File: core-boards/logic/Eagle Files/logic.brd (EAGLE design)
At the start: 94.2 x 80.9 mm, 78 parts, among them J1 S3B-VH, J2 B2PS-VH(LF)(SN), J3 B2PS-VH(LF)(SN), J4 B2PS-VH(LF)(SN), J5 B2PS-VH(LF)(SN), J6 B2PS-VH(LF)(SN), Q4 STT4P3LLH6, T1 R-78E5.0-1.0, U1 TC4427ACOA713, U2 TXB0106PWRPW16-M, U3 INA198AIDBVR, U4 TLV70233DBVR, U5 MCP2562-I/SN, U6 BMI088, U7 INA198AIDBVR, X1 MINI-USB_SHIELD5P4-32005-400, X10 S6B-EH(LF)(SN), X11 S3B-EH(LF)(SN), X12 B6B-EH-A(LF)(SN), X2 S5B-EH, X3 S5B-EH, X4 B6B-EH-A(LF)(SN), X7 SI-50170, X8 B6B-EH-A(LF)(SN), X9 B6B-EH-A(LF)(SN)

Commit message: logic board revision schemaitcs done
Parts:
- removed C14, C15: 100nF, rcl:C0603
- removed C3: 0.1uF, rcl:C0603
- removed R11: 120, rcl:R0603
- removed R15: 1k, rcl:R0603
- removed R16, R17: (no value), rcl:R0603
- removed U6: BMI088, IGVC-IC:BMI088
- removed X10: S6B-EH(LF)(SN), IGVC-Connector:S4BEHLFSN
- added J7: B2PS-VH(LF)(SN), RoboJackets-Connectors:B2PS-CENTERED
- R2: value 1M -> 10k
- U5: value MCP2562-I/SN -> MCP2551T-I/SN
- moved U5 72.2 mm to (-7.50, -10.2), turned to 0 degrees
- moved R2 69.7 mm to (-1.62, -3.62), turned to 0 degrees
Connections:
- removed net FAN_PWM: X10.X-1, X12.X-3
- removed net N$17: U6.P$14
- removed net N$3: J1.3
- new net NR: A1.4, J7.2, R2.1
- net +24V: no longer X10.X-3
- net +3V3: no longer C14.1, C15.1, C3.1, R16.2, R17.2, U5.5, U6.P$11, U6.P$3, U6.P$7
- net +5V: now also R2.2
- net CANH: now also X12.X-5; no longer R11.1
- net CANL: now also X12.X-6; no longer R11.2
- net CON_CONNECTED: no longer R15.2, X12.X-6
- net DIAG_RX: now also X12.X-4; no longer X12.X-5
- net DIAG_TX: now also X12.X-3; no longer X12.X-4
- net GND: now also J1.3, J7.1, U5.8; no longer C14.2, C15.2, C3.2, R15.1, R2.1, U6.P$10, U6.P$15, U6.P$2, U6.P$4, U6.P$6, X10.X-4
- net INT1_ACCEL: no longer U6.P$16
- net INT2_ACCEL: no longer U6.P$1
- net INT3_GYRO: no longer U6.P$12
- net INT4_GYRO: no longer U6.P$13
- net SAFETY_LIGHT: no longer R2.2
- net SCL_3V3: no longer R17.1, U6.P$9
- net SDA_3V3: no longer R16.1, U6.P$8
- net STANDBY: no longer U5.8
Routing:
- net FAN_PWM: track 41.8 -> 0.00 mm
- net +3V3: track 149.8 -> 118.7 mm, vias 11 -> 9
- net GND: track 66.4 -> 46.6 mm, vias 27 -> 20
- net SCL_3V3: track 26.4 -> 10.1 mm
- net CANH: track 14.1 -> 4.30 mm
- net SDA_3V3: track 23.9 -> 16.4 mm
- net INT1_ACCEL: track 7.50 -> 2.80 mm
- net INT2_ACCEL: track 5.64 -> 1.14 mm
- net DIAG_RX: track 59.6 -> 55.4 mm
- net CANL: track 15.8 -> 12.8 mm
- net CON_CONNECTED: track 46.8 -> 43.9 mm
- net DIAG_TX: track 65.5 -> 62.9 mm
- net MBED_CAN_TD: track 33.6 -> 32.1 mm
- net +24V: track 32.0 -> 30.5 mm
- net STANDBY: track 21.6 -> 20.3 mm
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
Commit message: logic board design for internal review :rocket:
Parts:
- removed X1: MINI-USB_SHIELD5P4-32005-400, con-cypressindustries:32005-400
- removed X11: S3B-EH(LF)(SN), IGVC-Connector:S3BEHLFSN
- added J8: B2PS-VH(LF)(SN), RoboJackets-Connectors:B2PS-CENTERED
- moved U5 69.7 mm to (56.2, 18.0), turned to 270 degrees
- moved J7 40.7 mm to (32.9, 8.38)
- moved R2 29.3 mm to (25.2, 8.00), turned to 180 degrees
- moved X12 12.1 mm to (56.2, 1.12)
- moved C12 1.27 mm to (67.4, 10.0), turned to 0 degrees
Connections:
- removed net CANH: U5.7, X11.TX, X12.X-5
- removed net CANL: U5.6, X11.RX, X12.X-6
- removed net CON_CONNECTED: A1.21
- removed net D_N: A1.32, X1.2
- removed net D_P: A1.31, X1.3
- removed net STANDBY: A1.22
- new net CAN_N: U5.6, X12.X-5
- new net CAN_P: U5.7, X12.X-6
- new net STATUS_LED1: A1.32, J8.2
- new net STATUS_LED2: A1.31, J8.1
- net +5V: no longer X1.1
- net GND: no longer X1.5, X11.GND
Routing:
- net NR: track 0.00 -> 85.6 mm, vias 0 -> 4
- net CON_CONNECTED: track 43.9 -> 0.00 mm, vias 2 -> 0
- net D_N: track 38.9 -> 0.00 mm
- net D_P: track 37.7 -> 0.00 mm
- net STATUS_LED2: track 0.00 -> 26.5 mm
- net CAN_P: track 0.00 -> 25.9 mm, vias 0 -> 1
- net CAN_N: track 0.00 -> 25.4 mm, vias 0 -> 1
- net STATUS_LED1: track 0.00 -> 23.6 mm
- net +3V3: track 118.7 -> 97.4 mm, vias 9 -> 7
- net STANDBY: track 20.3 -> 0.00 mm, vias 2 -> 0
- net DIAG_RX: track 55.4 -> 73.0 mm, vias 1 -> 2
- net DIAG_TX: track 62.9 -> 80.2 mm
- net INT4_GYRO: track 16.5 -> 0.00 mm, vias 2 -> 0
- net INT3_GYRO: track 14.0 -> 0.00 mm, vias 2 -> 0
- net CANL: track 12.8 -> 0.00 mm
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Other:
- board text added: "Diagnostic"
- board text removed: "CAN"
- board text removed: "FAN"

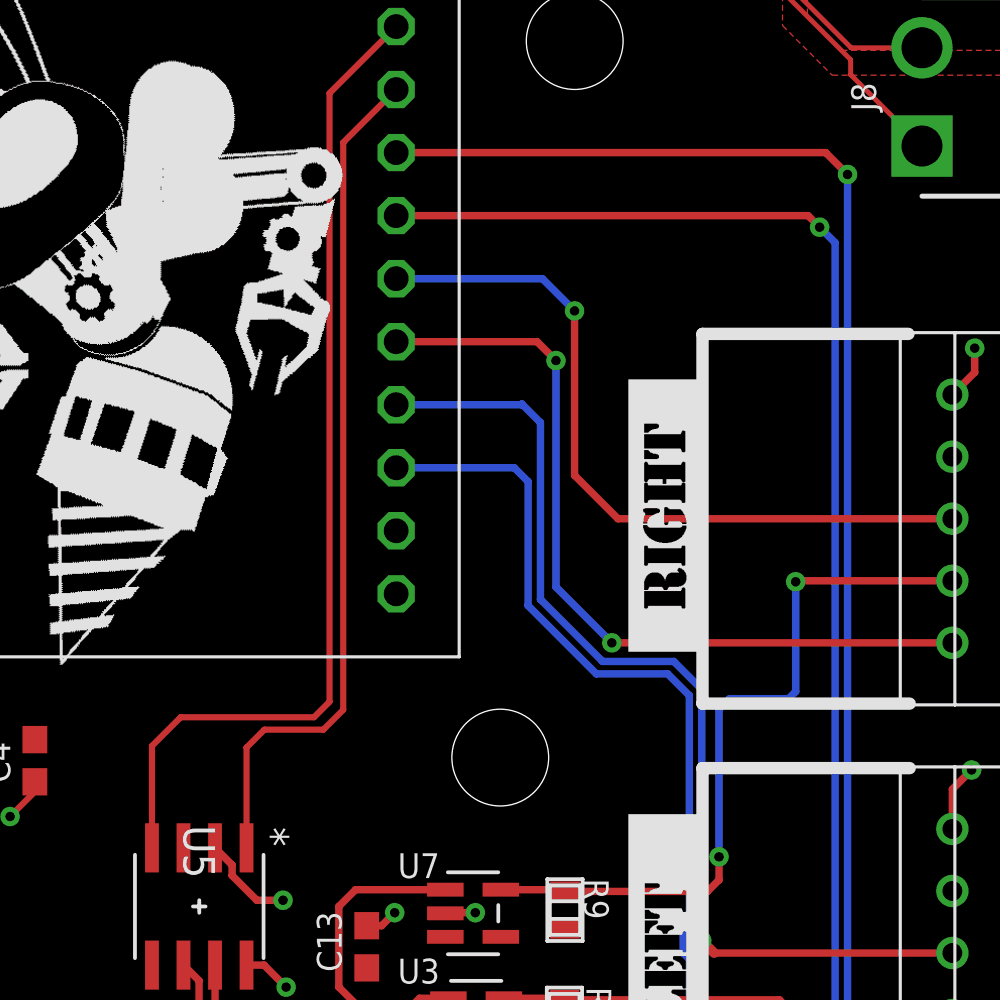
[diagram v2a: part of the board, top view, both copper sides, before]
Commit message: Pin inversion fix
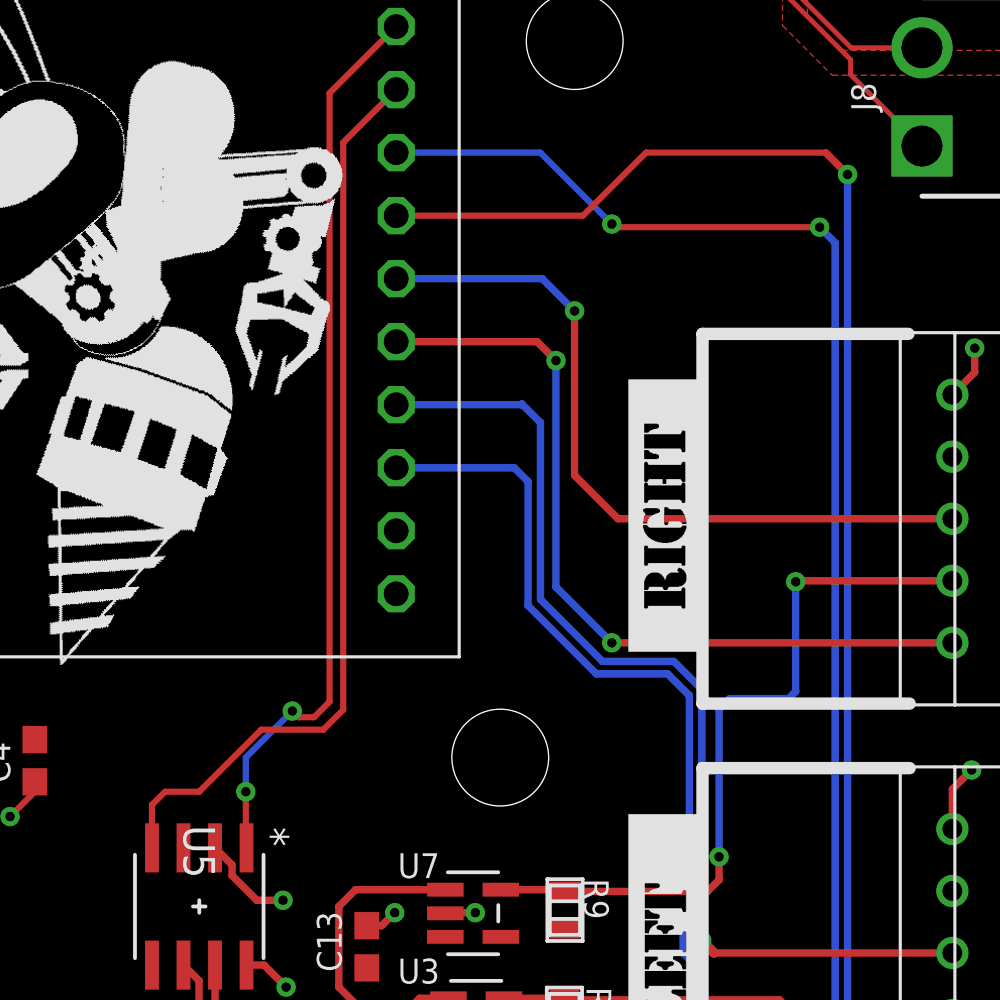
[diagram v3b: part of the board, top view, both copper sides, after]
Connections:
- net DIAG_RX: now also A1.28; no longer A1.27
- net DIAG_TX: now also A1.27; no longer A1.28
- net MBED_CAN_RD: now also U5.1; no longer U5.4
- net MBED_CAN_TD: now also U5.4; no longer U5.1
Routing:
- net MBED_CAN_RD: track 40.3 -> 36.5 mm, vias 0 -> 2
- net MBED_CAN_TD: track 34.4 -> 37.3 mm
- net DIAG_TX: track 80.2 -> 81.2 mm
- net DIAG_RX: track 73.0 -> 74.1 mm, vias 2 -> 3
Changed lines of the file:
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@@
 </signal>
 <signal name="DIAG_RX">
-<contactref element="A1" pad="27"/>
-<wire x1="64.185" y1="45.84" x2="80.785" y2="45.84" width="0.3" layer="1"/>
-<wire x1="80.785" y1="45.84" x2="81.25" y2="45.375" width="0.3" layer="1"/>
-<via x="81.25" y="45.375" extent="1-16" drill="0.381"/>
-<wire x1="81.25" y1="45.375" x2="81.875" y2="44.75" width="0.3" layer="16"/>
+<wire x1="81.875" y1="44.75" x2="81.25" y2="45.375" width="0.3" layer="16"/>
 <wire x1="81.875" y1="44.75" x2="81.875" y2="8.875" width="0.3" layer="16"/>
 <contactref element="X12" pad="X-4"/>
@@
 <wire x1="81.875" y1="8.875" x2="80.625" y2="7.625" width="0.3" layer="16"/>
 <wire x1="75.875" y1="2.375" x2="71.65255625" y2="2.375" width="0.3" layer="1"/>
+<contactref element="A1" pad="28"/>
+<via x="81.25" y="45.375" extent="1-16" drill="0.381"/>
+<wire x1="81.25" y1="45.375" x2="73" y2="45.375" width="0.25" layer="1"/>
+<wire x1="73" y1="45.375" x2="72.875" y2="45.5" width="0.25" layer="1"/>
+<via x="72.875" y="45.5" extent="1-16" drill="0.381"/>
+<wire x1="72.875" y1="45.5" x2="69.995" y2="48.38" width="0.25" layer="16"/>
+<wire x1="69.995" y1="48.38" x2="64.185" y2="48.38" width="0.25" layer="16"/>
 </signal>
 <signal name="DIAG_TX">
-<contactref element="A1" pad="28"/>
-<wire x1="64.185" y1="48.38" x2="81.495" y2="48.38" width="0.3" layer="1"/>
-<wire x1="81.495" y1="48.38" x2="82.375" y2="47.5" width="0.3" layer="1"/>
+<wire x1="82.375" y1="47.5" x2="81.495" y2="48.38" width="0.3" layer="1"/>
 <via x="82.375" y="47.5" extent="1-16" drill="0.381"/>
 <wire x1="82.375" y1="47.5" x2="82.375" y2="7.75" width="0.3" layer="16"/>
@@
 <wire x1="76.25" y1="1.625" x2="81.625" y2="7" width="0.3" layer="1"/>
 <wire x1="65.45" y1="1.625" x2="76.25" y2="1.625" width="0.3" layer="1"/>
+<contactref element="A1" pad="27"/>
+<wire x1="81.495" y1="48.38" x2="74.255" y2="48.38" width="0.25" layer="1"/>
+<wire x1="71.715" y1="45.84" x2="64.185" y2="45.84" width="0.25" layer="1"/>
+<wire x1="74.255" y1="48.38" x2="71.715" y2="45.84" width="0.25" layer="1"/>
 </signal>
 <signal name="MBED_CAN_RD">
 <contactref element="A1" pad="30"/>
 <wire x1="61.5" y1="50.775" x2="64.185" y2="53.46" width="0.25" layer="1"/>
-<wire x1="60.875" y1="25.625" x2="61.5" y2="26.25" width="0.25" layer="1"/>
-<wire x1="60.875" y1="25.625" x2="55.5" y2="25.625" width="0.25" layer="1"/>
+<wire x1="61.5" y1="26.25" x2="60.875" y2="25.625" width="0.25" layer="1"/>
 <wire x1="61.5" y1="26.25" x2="61.5" y2="50.775" width="0.25" layer="1"/>
-<contactref element="U5" pad="4"/>
-<wire x1="54.345" y1="24.47" x2="54.345" y2="20.3622" width="0.25" layer="1"/>
-<wire x1="55.5" y1="25.625" x2="54.345" y2="24.47" width="0.25" layer="1"/>
+<contactref element="U5" pad="1"/>
+<wire x1="60.875" y1="25.625" x2="60.25" y2="25.625" width="0.25" layer="1"/>
+<wire x1="60.25" y1="25.625" x2="60" y2="25.875" width="0.25" layer="1"/>
+<via x="60" y="25.875" extent="1-16" drill="0.381"/>
+<wire x1="60" y1="25.875" x2="58.125" y2="24" width="0.25" layer="16"/>
+<wire x1="58.125" y1="24" x2="58.125" y2="22.625" width="0.25" layer="16"/>
+<via x="58.125" y="22.625" extent="1-16" drill="0.381"/>
+<wire x1="58.125" y1="22.625" x2="58.125" y2="20.3922" width="0.25" layer="1"/>
+<wire x1="58.125" y1="20.3922" x2="58.155" y2="20.3622" width="0.25" layer="1"/>
 </signal>
 <signal name="MBED_CAN_TD">
@@
 <wire x1="62.0524" y1="25.9274" x2="61.25" y2="25.125" width="0.25" layer="1"/>
 <wire x1="62.0524" y1="48.7874" x2="62.0524" y2="25.9274" width="0.25" layer="1"/>
-<wire x1="61.25" y1="25.125" x2="58.875" y2="25.125" width="0.25" layer="1"/>
-<contactref element="U5" pad="1"/>
-<wire x1="58.155" y1="20.3622" x2="58.155" y2="24.405" width="0.25" layer="1"/>
-<wire x1="58.155" y1="24.405" x2="58.875" y2="25.125" width="0.25" layer="1"/>
+<contactref element="U5" pad="4"/>
+<wire x1="54.345" y1="20.3622" x2="54.345" y2="20.7545" width="0.25" layer="1"/>
+<wire x1="54.345" y1="21.22" x2="54.345" y2="21" width="0.25" layer="1"/>
+<wire x1="54.345" y1="21" x2="54.345" y2="20.3622" width="0.25" layer="1"/>
+<wire x1="58.75" y1="25.125" x2="56.25" y2="22.625" width="0.25" layer="1"/>
+<wire x1="56.25" y1="22.625" x2="54.875" y2="22.625" width="0.25" layer="1"/>
+<wire x1="54.875" y1="22.625" x2="54.345" y2="22.095" width="0.25" layer="1"/>
+<wire x1="54.345" y1="22.095" x2="54.345" y2="21.22" width="0.25" layer="1"/>
+<wire x1="61.25" y1="25.125" x2="58.75" y2="25.125" width="0.25" layer="1"/>
 </signal>
 <signal name="CAN_P">

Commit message: design rev
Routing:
- added copper zone on layer 1, net VBAT_24
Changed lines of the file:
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@@
 <wire x1="64.185" y1="56.1226" x2="64.185" y2="56" width="0.2" layer="1"/>
+</signal>
+<signal name="VBAT_24">
+<polygon width="0.1524" layer="1">
+<vertex x="49.25" y="63"/>
+<vertex x="59.625" y="64.25"/>
+<vertex x="59.625" y="57.5"/>
+<vertex x="56.75" y="54.625"/>
+<vertex x="49.25" y="62.125"/>
+</polygon>
 </signal>
 </signals>

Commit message: changes before design rev
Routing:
- removed copper zone on layer 1, net VBAT_24
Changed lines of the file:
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@@
 <wire x1="64.185" y1="56.1226" x2="64.185" y2="56" width="0.2" layer="1"/>
-</signal>
-<signal name="VBAT_24">
-<polygon width="0.1524" layer="1">
-<vertex x="49.25" y="63"/>
-<vertex x="59.625" y="64.25"/>
-<vertex x="59.625" y="57.5"/>
-<vertex x="56.75" y="54.625"/>
-<vertex x="49.25" y="62.125"/>
-</polygon>
 </signal>
 </signals>

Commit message: Routing rev finished
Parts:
- added C14, C15: 0.1uF, rcl:C0603
- added C3: 1uF, rcl:C0805
- added U6: D5V0L1B2WS-7, IGVC-Discrete:SOD323
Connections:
- new net N$3: C3.1, J7.1
- net +12V: now also U6.1
- net +3V3: no longer R5.2, U2.2
- net GND: now also C14.2, C15.2, C3.2, R5.2, U1.2, U2.2, U6.2; no longer J7.1, X7.C1, X7.C2
- net SCL_5V: now also C14.1
- net SDA_5V: now also C15.1
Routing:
- net +3V3: track 97.4 -> 73.3 mm, vias 7 -> 4
- net GND: track 49.4 -> 67.5 mm, vias 21 -> 26
- net N$3: track 0.00 -> 5.40 mm
- net SDA_5V: track 96.5 -> 101.7 mm, vias 3 -> 4
- net SCL_5V: track 99.2 -> 101.3 mm
